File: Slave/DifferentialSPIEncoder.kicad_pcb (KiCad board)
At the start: 2 copper layers, 26 parts, among them J1 debug, J2 8P8C_Shielded, U1 TLV71333PDBV, U2 AS5048A, U3 MAX485E, U4 MAX485E, U5 MAX485E

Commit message: new stuff
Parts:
- C1, C2, C4, C5, C6, C7, C8, C9: footprint Capacitor_SMD:C_0805_2012Metric_Pad1.15x1.40mm_HandSolder -> Capacitor_SMD:C_0402_1005Metric
- C3: footprint Capacitor_SMD:C_0805_2012Metric_Pad1.15x1.40mm_HandSolder -> Capacitor_SMD:C_0402_1005Metric; moved to B.Cu
- R1, R10, R2, R3, R4, R5, R6, R7, R8, R9: footprint Resistor_SMD:R_0805_2012Metric_Pad1.15x1.40mm_HandSolder -> Resistor_SMD:R_0402_1005Metric
- U2: moved to B.Cu
- moved R9 53.4 mm to (110.6, 66.2), turned to 90 degrees
- moved R1 49.4 mm to (112.6, 62.7)
- moved R10 48.2 mm to (110.5, 58.9), turned to 90 degrees
- moved R5 45.1 mm to (119.5, 59.5), turned to 90 degrees
- moved R7 44.0 mm to (120.0, 64.4), turned to 90 degrees
- moved R6 40.9 mm to (120.0, 66.4), turned to 180 degrees
- moved C9 38.7 mm to (110.5, 61.8), turned to 270 degrees
- moved R2 37.0 mm to (120.0, 67.6)
- moved R8 36.9 mm to (120.1, 71.4), turned to 180 degrees
- moved C2 35.5 mm to (127.5, 73.3), turned to 270 degrees
- moved C8 35.1 mm to (110.6, 73.5), turned to 90 degrees
- moved C1 34.6 mm to (121.5, 73.7), turned to 180 degrees
- moved C7 33.3 mm to (110.4, 68.3), turned to 270 degrees
- moved C3 32.8 mm to (107.8, 65.3), turned to 180 degrees
- moved R4 31.7 mm to (119.9, 69.1), turned to 180 degrees
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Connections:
- net /CLK_A renamed /CLK_+
- net /CLK_B renamed /CLK_-
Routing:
- net +5V: track 0.00 -> 27.3 mm, vias 0 -> 1
- net GND: track 0.00 -> 27.3 mm, vias 0 -> 14
- net CLK: track 0.00 -> 18.4 mm, vias 0 -> 1
- net +3V3: track 0.00 -> 17.7 mm, vias 0 -> 2
- net MISO: track 0.00 -> 16.0 mm, vias 0 -> 1
- net ~CSn: track 0.00 -> 16.0 mm, vias 0 -> 1
- net /CLK_-: track 0.00 -> 15.3 mm, vias 0 -> 1
- net /CLK_+: track 0.00 -> 15.3 mm, vias 0 -> 1
- net (no net): track 0.00 -> 6.06 mm
- net Net-(R1-Pad2): track 0.00 -> 5.79 mm, vias 0 -> 1
- net Net-(R7-Pad1): track 0.00 -> 4.13 mm
- net /MISO_-: track 16.1 -> 12.5 mm
- net Net-(C6-Pad1): track 0.00 -> 3.52 mm
- net Net-(R8-Pad2): track 0.00 -> 3.41 mm
- net Net-(R5-Pad1): track 0.00 -> 3.21 mm
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- added copper zone on F.Cu, net +3V3
- added copper zone on B.Cu, net GND
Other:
- board outline added: 35.6 x 21.6 mm

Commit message: nother commit
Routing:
- net /CS_+: track 11.2 -> 12.4 mm
- net /MISO_-: track 12.5 -> 13.5 mm

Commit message: next version
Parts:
- added C10: 10uF, Capacitor_SMD:C_0603_1608Metric, B.Cu at (107.2, 66.3)
- moved J1 5.86 mm to (128.1, 57.5)
- moved R10 0.49 mm to (110.5, 59.4)
- moved C3 0.38 mm to (107.5, 65.0)
- moved C2 0.25 mm to (127.3, 73.3)
- moved U5 0.11 mm to (114.8, 59.5)
- moved R1 0.10 mm to (112.6, 62.8)
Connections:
- J2 pad SH: GND -> Net-(J2-PadSH)
- R6 pad 1: +3V3 -> ~CSn
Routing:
- net +3V3: track 17.7 -> 27.5 mm, vias 2 -> 3
- net ~CSn: track 16.0 -> 22.3 mm
- net (no net): track 6.06 -> 0.00 mm, vias 0 -> 3
- net MISO: track 16.0 -> 20.0 mm
- net GND: track 27.3 -> 23.6 mm
- net CLK: track 18.4 -> 16.5 mm
- net /CLK_-: track 15.3 -> 14.6 mm
- net +5V: track 27.3 -> 26.7 mm
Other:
- board size 35.6 x 21.6 mm -> 35.6 x 25.4 mm

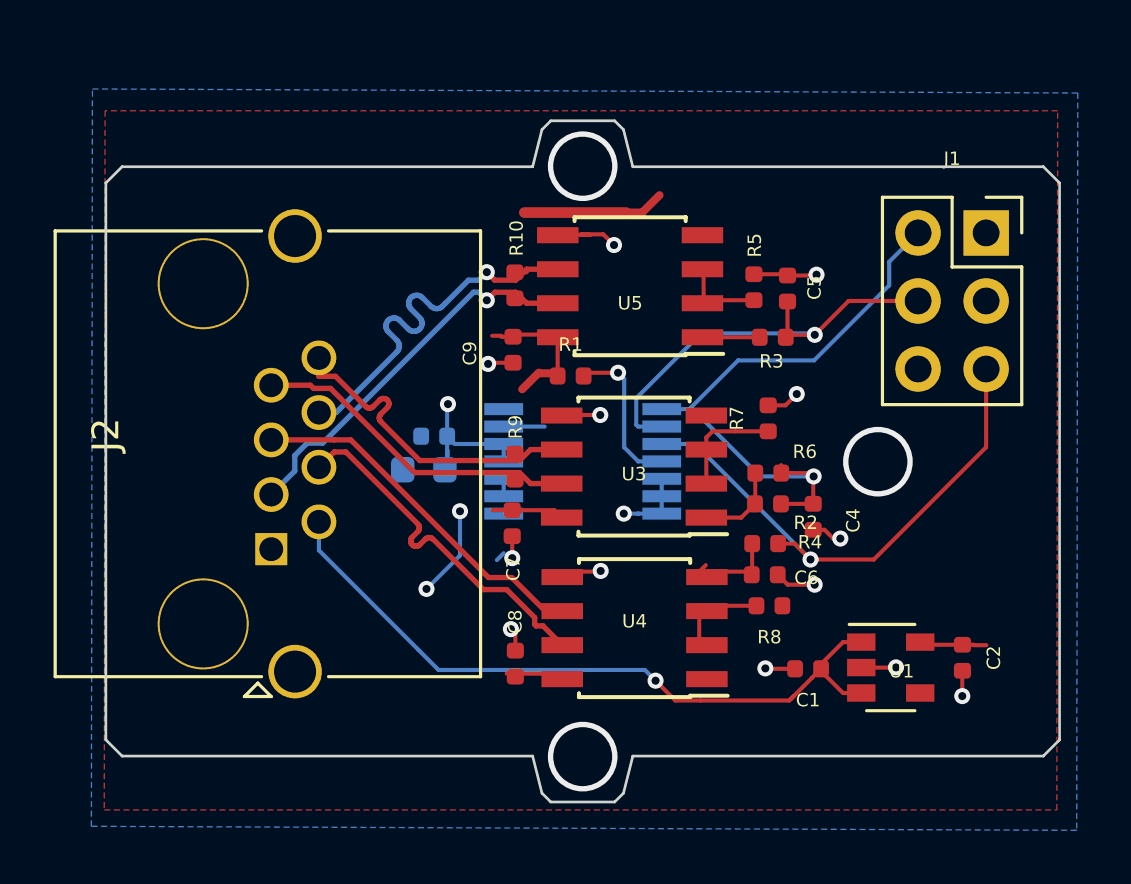
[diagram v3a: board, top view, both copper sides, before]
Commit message: fixed mounting holes
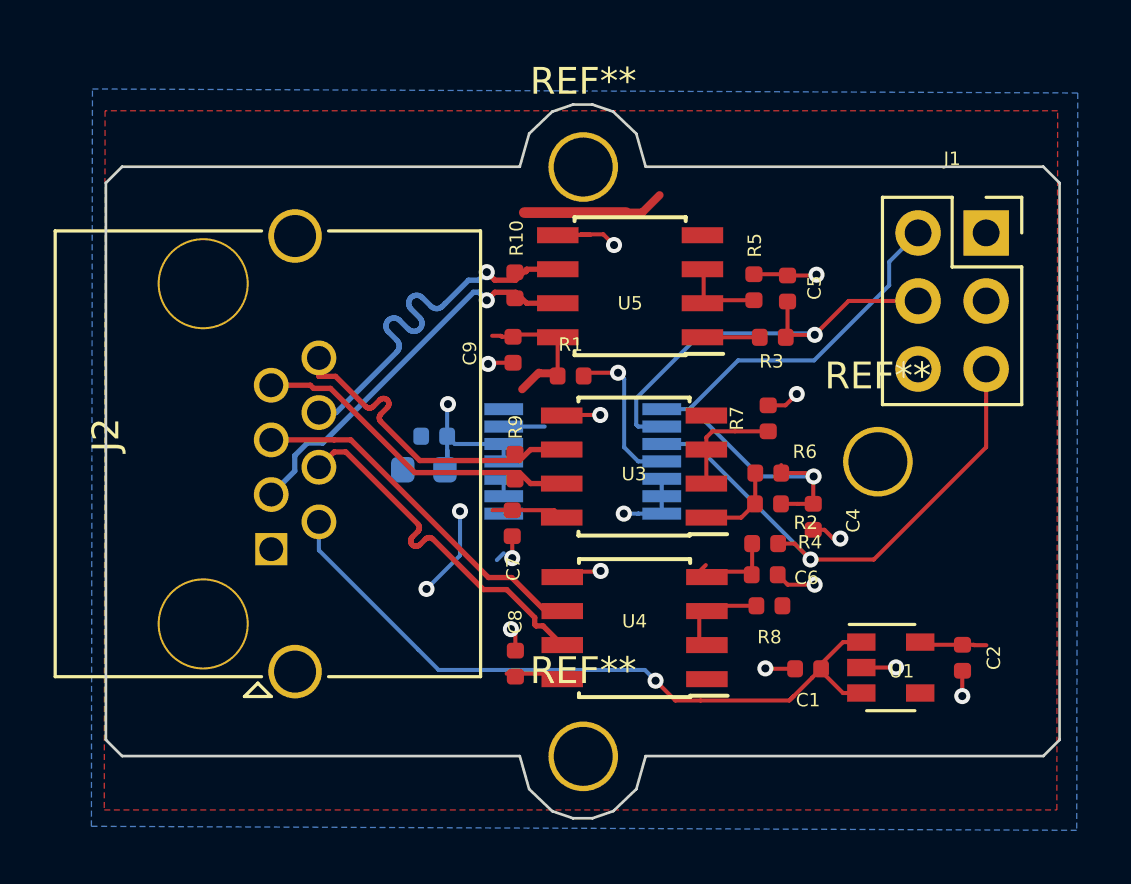
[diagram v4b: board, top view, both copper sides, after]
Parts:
- added REF**: MountingHole_MINE, MountingHole:MountingHole_MINE, F.Cu at (113.1, 77.0)
- added REF**: MountingHole_MINE, MountingHole:MountingHole_MINE, F.Cu at (124.1, 66.0)
- added REF**: MountingHole_MINE, MountingHole:MountingHole_MINE, F.Cu at (113.1, 55.0)
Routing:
- net (no net): vias 3 -> 0
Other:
- board size 35.6 x 25.4 mm -> 35.6 x 26.6 mm
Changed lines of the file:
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@@
   (general
     (thickness 1.6)
-    (drawings 20)
-    (tracks 363)
+    (drawings 24)
+    (tracks 360)
     (zones 0)
-    (modules 27)
+    (modules 30)
     (nets 27)
   )
@@
   (layers
     (0 F.Cu signal)
-    (31 B.Cu signal)
+    (31 B.Cu signal hide)
     (32 B.Adhes user hide)
-    (33 F.Adhes user)
-    (34 B.Paste user)
-    (35 F.Paste user)
+    (33 F.Adhes user hide)
+    (34 B.Paste user hide)
+    (35 F.Paste user hide)
     (36 B.SilkS user hide)
     (37 F.SilkS user hide)
     (38 B.Mask user hide)
-    (39 F.Mask user)
+    (39 F.Mask user hide)
     (40 Dwgs.User user hide)
     (41 Cmts.User user hide)
@@
     (46 B.CrtYd user hide)
     (47 F.CrtYd user hide)
-    (48 B.Fab user hide)
+    (48 B.Fab user)
     (49 F.Fab user hide)
   )
@@
     )
   )
+  (module MountingHole:MountingHole_MINE (layer F.Cu)
+    (at 113.1 77)
+    (descr "Mounting Hole 2.2mm, M2")
+    (tags "mounting hole 2.2mm m2")
+    (attr virtual)
+    (fp_text reference REF** (at 0 -3.2) (layer F.SilkS)
+      (effects (font (size 1 1) (thickness 0.15)))
+    )
+    (fp_text value MountingHole_MINE (at 0 3.2) (layer F.Fab)
+      (effects (font (size 1 1) (thickness 0.15)))
+    )
+    (fp_circle (center 0 0) (end 2.45 0) (layer F.CrtYd) (width 0.05))
+    (fp_circle (center 0 0) (end 2.2 0) (layer Cmts.User) (width 0.15))
+    (fp_text user %R (at 0.3 0) (layer F.Fab)
+      (effects (font (size 1 1) (thickness 0.15)))
+    )
+    (pad 1 thru_hole circle (at 0 0) (size 2.6 2.6) (drill 2.2) (layers *.Cu *.Mask))
+  )
+  (module MountingHole:MountingHole_MINE (layer F.Cu)
+    (at 124.1 66)
+    (descr "Mounting Hole 2.2mm, M2")
+    (tags "mounting hole 2.2mm m2")
+    (attr virtual)
+    (fp_text reference REF** (at 0 -3.2) (layer F.SilkS)
+      (effects (font (size 1 1) (thickness 0.15)))
+    )
+    (fp_text value MountingHole_MINE (at 0 3.2) (layer F.Fab)
+      (effects (font (size 1 1) (thickness 0.15)))
+    )
+    (fp_circle (center 0 0) (end 2.45 0) (layer F.CrtYd) (width 0.05))
+    (fp_circle (center 0 0) (end 2.2 0) (layer Cmts.User) (width 0.15))
+    (fp_text user %R (at 0.3 0) (layer F.Fab)
+      (effects (font (size 1 1) (thickness 0.15)))
+    )
+    (pad 1 thru_hole circle (at 0 0) (size 2.6 2.6) (drill 2.2) (layers *.Cu *.Mask))
+  )
+  (module MountingHole:MountingHole_MINE (layer F.Cu)
+    (at 113.1 55)
+    (descr "Mounting Hole 2.2mm, M2")
+    (tags "mounting hole 2.2mm m2")
+    (attr virtual)
+    (fp_text reference REF** (at 0 -3.2) (layer F.SilkS)
+      (effects (font (size 1 1) (thickness 0.15)))
+    )
+    (fp_text value MountingHole_MINE (at 0 3.2) (layer F.Fab)
+      (effects (font (size 1 1) (thickness 0.15)))
+    )
+    (fp_circle (center 0 0) (end 2.45 0) (layer F.CrtYd) (width 0.05))
+    (fp_circle (center 0 0) (end 2.2 0) (layer Cmts.User) (width 0.15))
+    (fp_text user %R (at 0.3 0) (layer F.Fab)
+      (effects (font (size 1 1) (thickness 0.15)))
+    )
+    (pad 1 thru_hole circle (at 0 0) (size 2.6 2.6) (drill 2.2) (layers *.Cu *.Mask))
+  )
   (module Capacitor_SMD:C_0603_1608Metric (layer B.Cu)
     (at 107.15 66.3 180)
@@
     )
   )
+  (gr_line (start 115.081864 78.221693) (end 115.431 76.9892) (layer Edge.Cuts) (width 0.1))
+  (gr_line (start 114.22165 79.043808) (end 115.081864 78.221693) (layer Edge.Cuts) (width 0.1))
+  (gr_line (start 113.44378 79.311029) (end 114.22165 79.043808) (layer Edge.Cuts) (width 0.1))
+  (gr_line (start 112.718219 79.311029) (end 113.44378 79.311029) (layer Edge.Cuts) (width 0.1))
+  (gr_line (start 111.940349 79.043808) (end 112.718219 79.311029) (layer Edge.Cuts) (width 0.1))
+  (gr_line (start 111.080135 78.221693) (end 111.940349 79.043808) (layer Edge.Cuts) (width 0.1))
+  (gr_line (start 110.731 76.9892) (end 111.080135 78.221693) (layer Edge.Cuts) (width 0.1))
+  (gr_line (start 95.886172 76.9892) (end 110.731 76.9892) (layer Edge.Cuts) (width 0.1))
+  (gr_line (start 95.280149 76.383177) (end 95.886172 76.9892) (layer Edge.Cuts) (width 0.1))
+  (gr_line (start 95.280149 55.595222) (end 95.280149 76.383177) (layer Edge.Cuts) (width 0.1))
   (gr_line (start 95.886172 54.9892) (end 95.280149 55.595222) (layer Edge.Cuts) (width 0.1))
-  (gr_line (start 111.210945 54.9892) (end 95.886172 54.9892) (layer Edge.Cuts) (width 0.1))
-  (gr_line (start 111.559943 53.602548) (end 111.210945 54.9892) (layer Edge.Cuts) (width 0.1))
-  (gr_line (start 111.890488 53.274928) (end 111.559943 53.602548) (layer Edge.Cuts) (width 0.1))
-  (gr_line (start 114.271511 53.274928) (end 111.890488 53.274928) (layer Edge.Cuts) (width 0.1))
-  (gr_line (start 114.602056 53.602548) (end 114.271511 53.274928) (layer Edge.Cuts) (width 0.1))
-  (gr_line (start 114.951054 54.9892) (end 114.602056 53.602548) (layer Edge.Cuts) (width 0.1))
-  (gr_line (start 130.275827 54.9892) (end 114.951054 54.9892) (layer Edge.Cuts) (width 0.1))
+  (gr_line (start 110.731 54.9892) (end 95.886172 54.9892) (layer Edge.Cuts) (width 0.1))
+  (gr_line (start 111.080135 53.756706) (end 110.731 54.9892) (layer Edge.Cuts) (width 0.1))
+  (gr_line (start 111.940349 52.934591) (end 111.080135 53.756706) (layer Edge.Cuts) (width 0.1))
+  (gr_line (start 112.718219 52.66737) (end 111.940349 52.934591) (layer Edge.Cuts) (width 0.1))
+  (gr_line (start 113.44378 52.66737) (end 112.718219 52.66737) (layer Edge.Cuts) (width 0.1))
+  (gr_line (start 114.22165 52.934591) (end 113.44378 52.66737) (layer Edge.Cuts) (width 0.1))
+  (gr_line (start 115.081864 53.756706) (end 114.22165 52.934591) (layer Edge.Cuts) (width 0.1))
+  (gr_line (start 115.431 54.9892) (end 115.081864 53.756706) (layer Edge.Cuts) (width 0.1))
+  (gr_line (start 130.275827 54.9892) (end 115.431 54.9892) (layer Edge.Cuts) (width 0.1))
   (gr_line (start 130.881849 55.595222) (end 130.275827 54.9892) (layer Edge.Cuts) (width 0.1))
   (gr_line (start 130.881849 76.383177) (end 130.881849 55.595222) (layer Edge.Cuts) (width 0.1))
   (gr_line (start 130.275827 76.9892) (end 130.881849 76.383177) (layer Edge.Cuts) (width 0.1))
-  (gr_line (start 114.951054 76.9892) (end 130.275827 76.9892) (layer Edge.Cuts) (width 0.1))
-  (gr_line (start 114.602056 78.375851) (end 114.951054 76.9892) (layer Edge.Cuts) (width 0.1))
-  (gr_line (start 114.271511 78.703471) (end 114.602056 78.375851) (layer Edge.Cuts) (width 0.1))
-  (gr_line (start 111.890488 78.703471) (end 114.271511 78.703471) (layer Edge.Cuts) (width 0.1))
-  (gr_line (start 111.559943 78.375851) (end 111.890488 78.703471) (layer Edge.Cuts) (width 0.1))
-  (gr_line (start 111.210945 76.9892) (end 111.559943 78.375851) (layer Edge.Cuts) (width 0.1))
-  (gr_line (start 95.886172 76.9892) (end 111.210945 76.9892) (layer Edge.Cuts) (width 0.1))
-  (gr_line (start 95.280149 76.383177) (end 95.886172 76.9892) (layer Edge.Cuts) (width 0.1))
-  (gr_line (start 95.280149 55.595222) (end 95.280149 76.383177) (layer Edge.Cuts) (width 0.1))
-  (via (at 113.08 54.97) (size 2.6) (drill 2.2) (layers F.Cu B.Cu) (net 0))
-  (via (at 113.08 77.01) (size 2.6) (drill 2.2) (layers F.Cu B.Cu) (net 0))
-  (via (at 124.1 66) (size 2.6) (drill 2.2) (layers F.Cu B.Cu) (net 0))
-  (via (at 107.25 70.75) (size 0.6) (drill 0.3) (layers F.Cu B.Cu) (net 3))
+  (gr_line (start 115.431 76.9892) (end 130.275827 76.9892) (layer Edge.Cuts) (width 0.1))
   (segment (start 121.97828 73.55428) (end 121.97828 73.73112) (width 0.1524) (layer F.Cu) (net 1))
   (segment (start 122.79716 72.7354) (end 121.97828 73.55428) (width 0.1524) (layer F.Cu) (net 1))
@@
   (segment (start 110.5662 72.4162) (end 110.4 72.25) (width 0.1524) (layer F.Cu) (net 2))
   (segment (start 110.5662 73.05308) (end 110.5662 72.4162) (width 0.1524) (layer F.Cu) (net 2))
+  (via (at 107.25 70.75) (size 0.6) (drill 0.3) (layers F.Cu B.Cu) (net 3))
   (segment (start 110.9 56.7) (end 114.7 56.7) (width 0.4) (layer F.Cu) (net 3))
   (segment (start 114.7 56.7) (end 114.8 56.7) (width 0.1524) (layer F.Cu) (net 3))
   (segment (start 110.8202 63.2968) (end 111.4425 62.6745) (width 0.3) (layer F.Cu) (net 3))
   (segment (start 112.0318 73.914) (end 110.24108 73.914) (width 0.1524) (layer F.Cu) (net 3))
-  (segment (start 120.49252 66.42608) (end 120.49252 66.12636) (width 0.1524) (layer F.Cu) (net 4))
   (segment (start 125.7788 72.83464) (end 125.67956 72.7354) (width 0.1524) (layer F.Cu) (net 3))
   (segment (start 127.508 72.83464) (end 125.7788 72.83464) (width 0.1524) (layer F.Cu) (net 3))
-  (segment (start 120.49252 66.42608) (end 120.88752 66.42608) (width 0.1524) (layer F.Cu) (net 4))
-  (segment (start 120.88752 66.42608) (end 121.62028 66.42608) (width 0.1524) (layer F.Cu) (net 4))
   (segment (start 110.5614 61.25464) (end 110.47984 61.3362) (width 0.1524) (layer F.Cu) (net 3))
   (segment (start 112.19436 61.25464) (end 110.5614 61.25464) (width 0.1524) (layer F.Cu) (net 3))
@@
   (segment (start 110.02364 61.3) (end 109.7 61.3) (width 0.1524) (layer F.Cu) (net 3))
   (segment (start 110.44936 67.81052) (end 109.71052 67.81052) (width 0.1524) (layer F.Cu) (net 3))
+  (segment (start 120.49252 66.42608) (end 120.49252 66.12636) (width 0.1524) (layer F.Cu) (net 4))
+  (segment (start 120.49252 66.42608) (end 120.88752 66.42608) (width 0.1524) (layer F.Cu) (net 4))
+  (segment (start 120.88752 66.42608) (end 121.62028 66.42608) (width 0.1524) (layer F.Cu) (net 4))
   (segment (start 121.70128 67.57416) (end 121.82856 67.44688) (width 0.1524) (layer F.Cu) (net 4))
   (segment (start 120.48208 67.57416) (end 121.11228 67.57416) (width 0.1524) (layer F.Cu) (net 4))

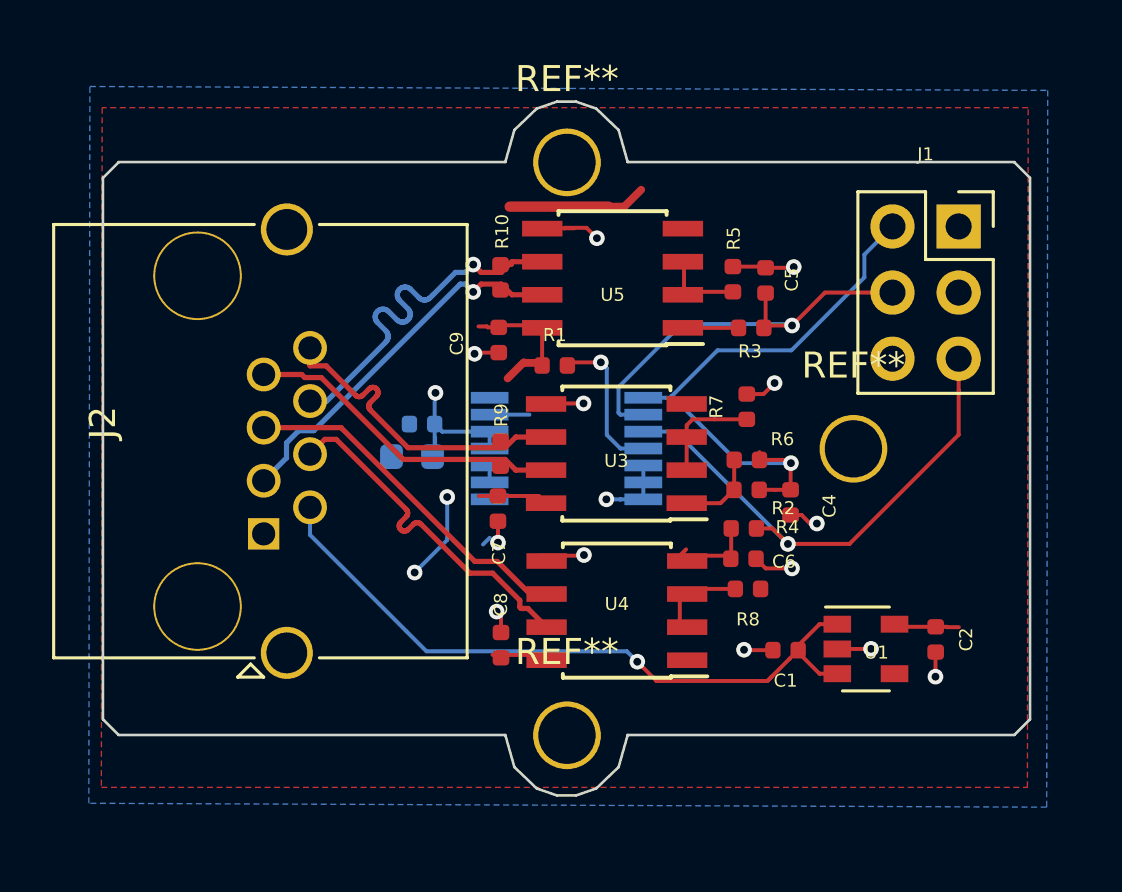
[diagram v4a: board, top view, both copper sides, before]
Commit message: converted to +5v only
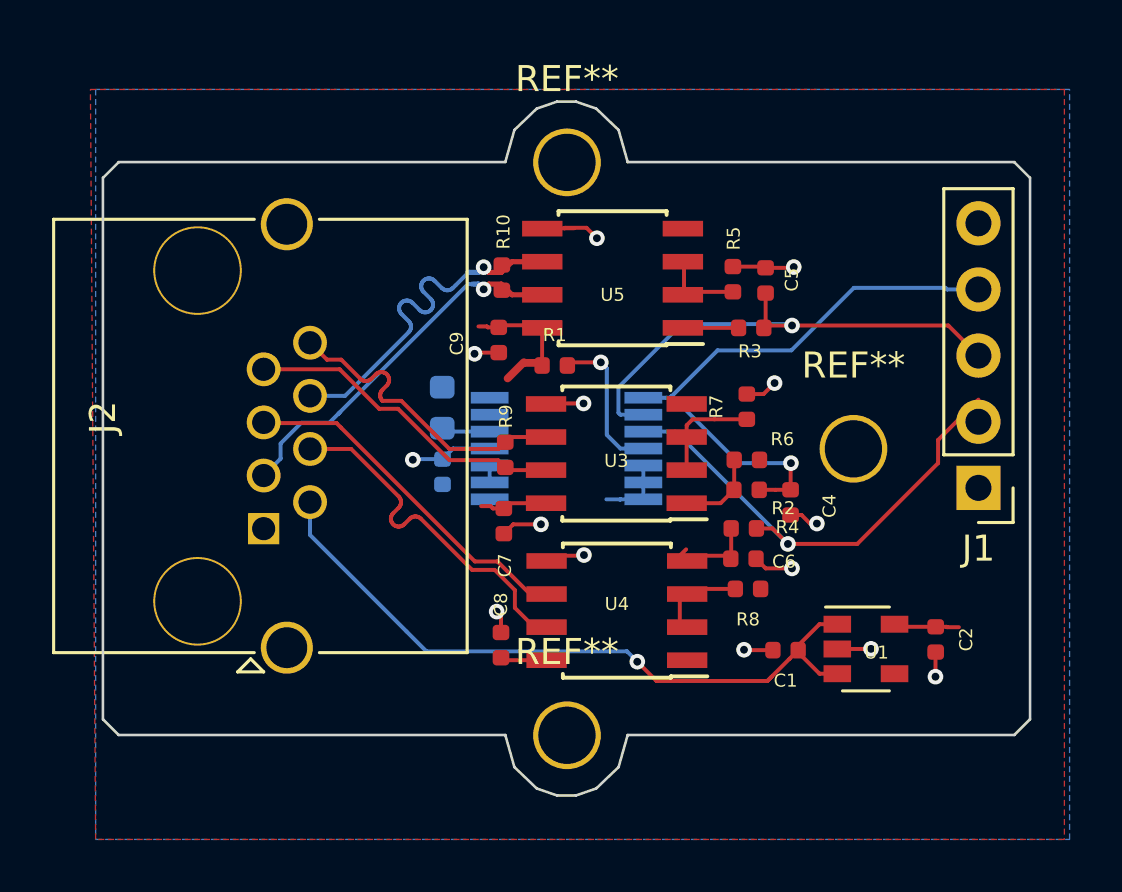
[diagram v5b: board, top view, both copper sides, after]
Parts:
- removed C10: 10uF, Capacitor_SMD:C_0603_1608Metric
- added C1: 10uF, Capacitor_SMD:C_0603_1608Metric, B.Cu at (108.3, 64.4)
- J1: value debug -> Conn_01x05_Male; footprint Connector_PinSocket_2.54mm:PinSocket_2x03_P2.54mm_Vertical -> Connector_PinHeader_2.54mm:PinHeader_1x05_P2.54mm_Vertical
- moved J1 10.1 mm to (128.9, 67.5), turned to 180 degrees
- moved C3 1.99 mm to (108.3, 66.9), turned to 270 degrees
- moved C7 0.53 mm to (110.7, 68.8)
- moved J2 0.20 mm to (101.5, 69.1)
- moved R9 0.19 mm to (110.7, 66.2)
- moved R10 0.05 mm to (110.6, 59.4)
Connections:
- C3 pad 1: +3V3 -> +5V
- C7 pad 1: +3V3 -> +5V
- C8 pad 1: +3V3 -> +5V
- C9 pad 1: +3V3 -> +5V
- J1 pad 1: +3V3 -> GND
- J1 pad 2: ~CSn -> MISO
- J1 pad 3: GND -> CLK
- J1 pad 4: CLK -> ~CSn
- J1 pad 5: MISO -> +5V
- R1 pad 1: +3V3 -> +5V
- R6 pad 1: ~CSn -> +5V
- R8 pad 1: +3V3 -> +5V
- U2 pad 11: +3V3 -> +5V
- U2 pad 12: +3V3 -> V3cap
- U3 pad 8: +3V3 -> +5V
- U4 pad 8: +3V3 -> +5V
- U5 pad 8: +3V3 -> +5V
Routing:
- net +3V3: track 27.5 -> 2.77 mm, vias 3 -> 0
- net +5V: track 26.7 -> 39.9 mm, vias 1 -> 2
- net CLK: track 16.5 -> 19.8 mm
- net V3cap: track 0.00 -> 1.87 mm
- net GND: track 23.6 -> 22.5 mm, vias 14 -> 13
- net MISO: track 20.0 -> 18.9 mm
- net /CLK_+: track 15.1 -> 14.2 mm
- net /CS_-: track 12.4 -> 12.9 mm
- added copper zone on F.Cu, net +5V
- removed copper zone on F.Cu, net +3V3
